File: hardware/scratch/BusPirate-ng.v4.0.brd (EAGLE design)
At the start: 100 x 50 mm, 136 parts, among them CON1 CON-USB-F-MICRO-B, IC10 74LVC1G07DBV, IC11 IC_BUFF_SN74LVC1T45DBV, IC12 74LVC1G07DBV, IC13 IC_BUFF_SN74LVC1T45DBV, IC14 74LVC1G07DBV, IC15 IC_BUFF_SN74LVC1T45DBV, IC16 74LVC1G07DBV, IC17 IC_BUFF_SN74LVC1T45DBV, IC2 IC_MEM_23LC1024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

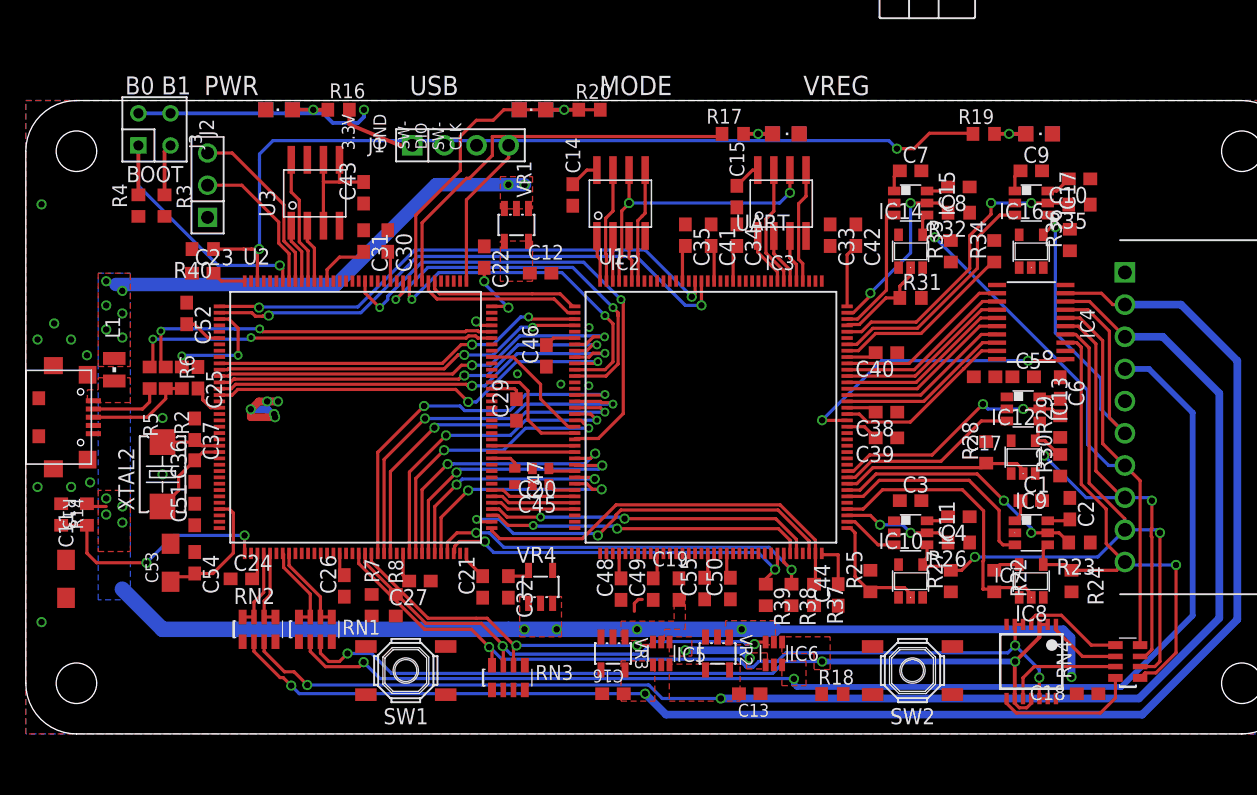
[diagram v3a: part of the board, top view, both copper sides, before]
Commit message: moving some pins and continue routing -move VREGEN from MCU pin PE1 to PD2 -move LD1 from MCU PD2 to PA15
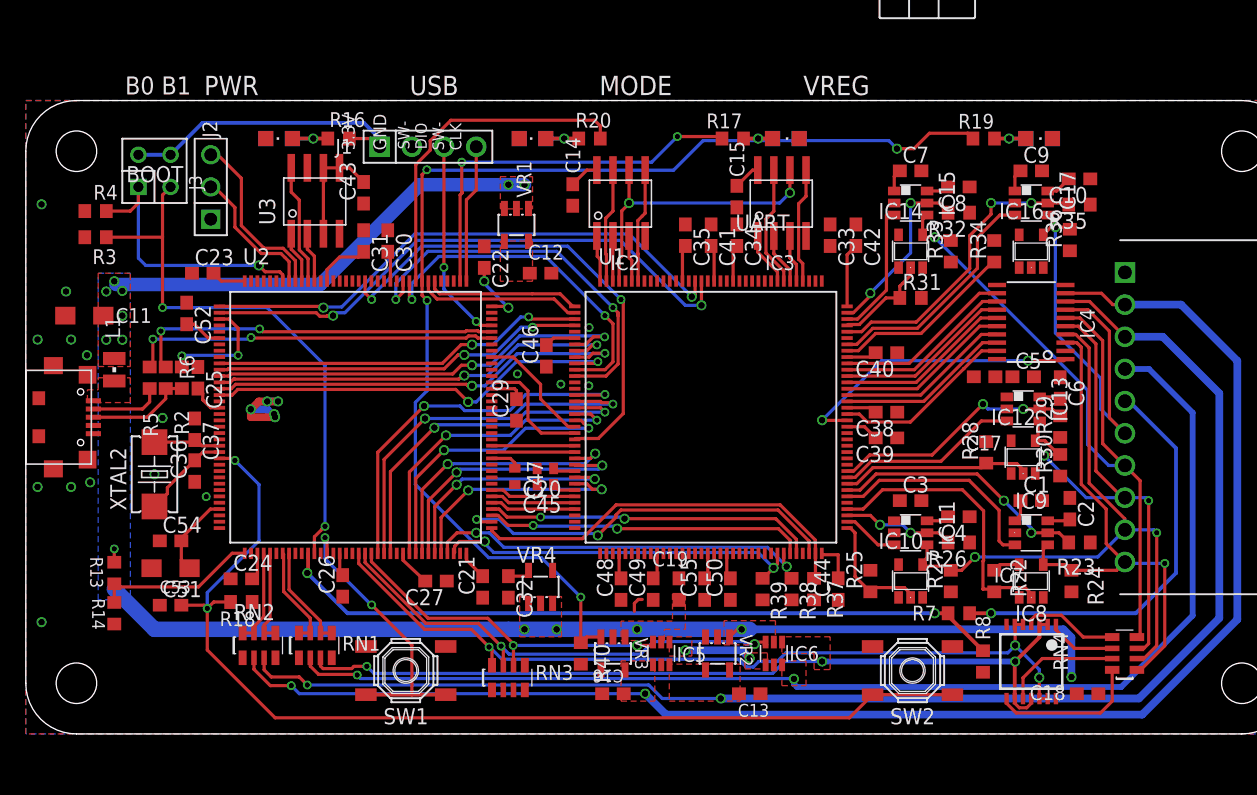
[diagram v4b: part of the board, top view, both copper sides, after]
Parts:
- moved R18 47.2 mm to (17.0, 10.4), turned to 0 degrees
- moved R8 46.6 mm to (75.6, 5.71)
- moved R7 46.4 mm to (73.7, 9.53), turned to 180 degrees
- moved R40 43.7 mm to (43.8, 6.35), turned to 270 degrees
- moved C11 20.8 mm to (4.62, 33.0), turned to 180 degrees
- moved R14 8.85 mm to (6.99, 9.53), turned to 90 degrees
- moved C51 7.41 mm to (11.4, 10.2), turned to 0 degrees
- moved R3 5.99 mm to (5.51, 39.2), turned to 180 degrees
- moved R13 5.10 mm to (6.99, 12.7)
- moved R4 3.41 mm to (5.51, 41.3), turned to 180 degrees
- moved J3 3.27 mm to (10.2, 44.5)
- moved C54 2.57 mm to (11.4, 15.2), turned to 0 degrees
- moved J1 2.57 mm to (27.9, 46.4)
- moved LED1 2.27 mm to (20.0, 47.0)
- moved LED2 2.27 mm to (20.0, 47.0)
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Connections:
- removed net N$47: U2.110
- new net N$15: U2.54
- net LD1: now also U2.110; no longer U2.116
- net USBLED: now also U2.111
- net VREGEN: now also U2.116; no longer U2.142
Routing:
- net RST: track 0.00 -> 84.7 mm, vias 0 -> 2
- net ADC1: track 0.00 -> 57.6 mm, vias 0 -> 2
- net BOOT1: track 4.10 -> 44.1 mm, vias 0 -> 2
- net IO_ADC/DAC: track 0.00 -> 33.0 mm, vias 0 -> 1
- net MS0: track 0.00 -> 22.9 mm, vias 0 -> 2
- net VREGEN: track 71.3 -> 92.7 mm, vias 2 -> 4
- net SWDIO: track 1.39 -> 16.2 mm, vias 1 -> 2
- net 3V3: track 129.5 -> 122.8 mm, vias 7 -> 6
- net ADC5: track 19.3 -> 13.0 mm, vias 2 -> 0
- net BPIO_MOSI: track 43.1 -> 41.1 mm
- net USBLED: track 24.8 -> 26.8 mm
- net FSMC_NWE_WE: track 29.8 -> 31.6 mm
- net FSMC_NOE_OE: track 26.3 -> 28.0 mm
- net VUSB: track 116.8 -> 118.1 mm, vias 17 -> 14
- net ADC4: track 6.23 -> 7.50 mm
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
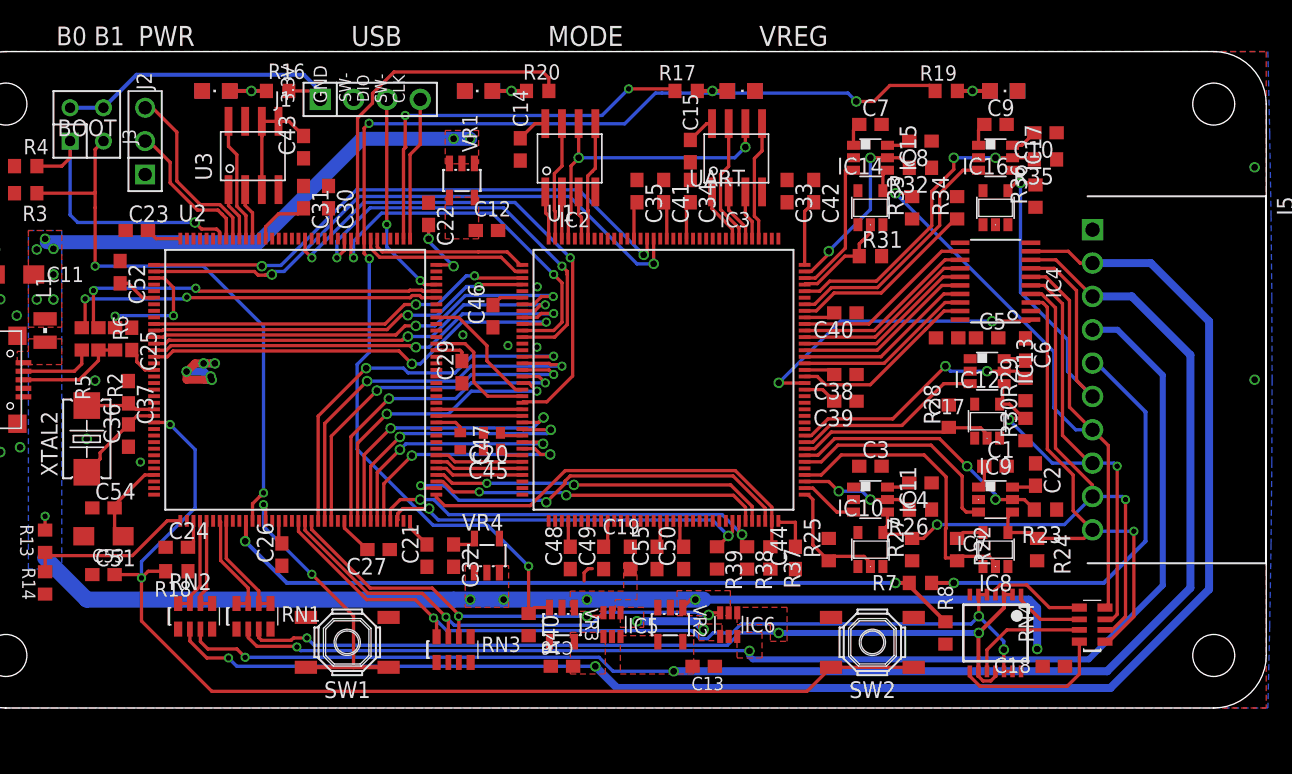
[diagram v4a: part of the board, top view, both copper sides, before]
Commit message: route power traces
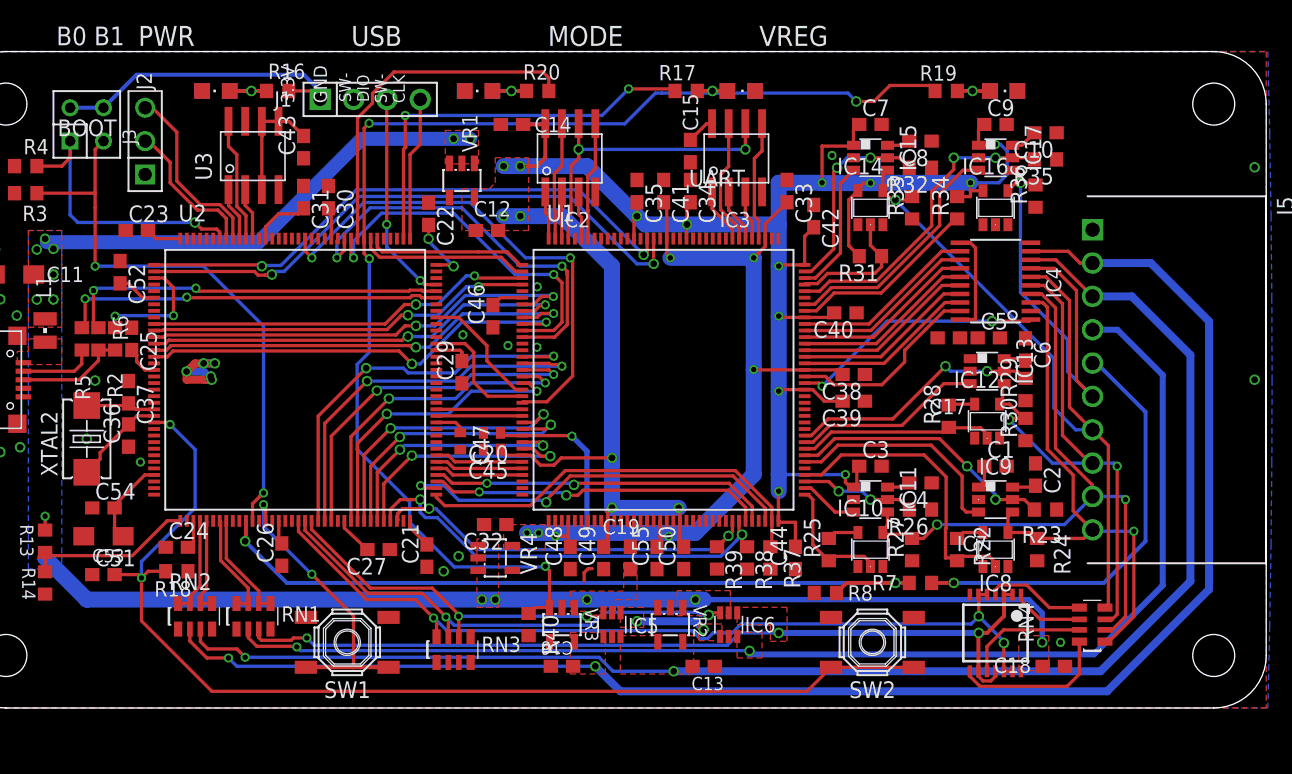
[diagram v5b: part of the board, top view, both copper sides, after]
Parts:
- moved R8 9.64 mm to (66.4, 8.76), turned to 0 degrees
- moved C32 3.96 mm to (41.3, 14.0), turned to 180 degrees
- moved C14 2.01 mm to (42.5, 44.5), turned to 180 degrees
- moved C42 1.90 mm to (65.5, 37.5)
- moved VR4 0.66 mm to (41.3, 11.4), turned to 270 degrees
- moved C38 0.64 mm to (68.6, 25.4)
- moved C39 0.64 mm to (68.6, 23.4)
- moved C17 0.13 mm to (75.8, 28.2)
- moved C5 0.13 mm to (78.9, 28.2)
- turned R31 to 180 degrees
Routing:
- net 3V3: track 122.8 -> 281.8 mm, vias 6 -> 24
- net 1V2: track 13.3 -> 79.8 mm, vias 0 -> 8
- net LAT_OE: track 23.2 -> 19.4 mm
- net BUFOD_CS: track 7.80 -> 9.98 mm
- net FPGA_CRESET: track 31.3 -> 33.3 mm
- net VREGEN: track 92.7 -> 94.6 mm
- net VUSB: track 118.1 -> 116.8 mm
- net BUFDIR_CS: track 14.4 -> 15.4 mm
- net ADC1: track 57.6 -> 58.5 mm
- net FPGA_CDONE: track 29.4 -> 30.1 mm
- net LAT_AUX1: track 14.4 -> 14.9 mm
- net GND: vias 19 -> 23
- added copper zone on layer 1, net 1V2
